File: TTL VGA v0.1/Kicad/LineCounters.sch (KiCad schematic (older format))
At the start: 17 parts

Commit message: tweaks
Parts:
- removed U? (x2): G22V10, symbol Logic_Programmable:PAL20RS10
- added U1, U5: G22V10, symbol 22V10:G22V10
- gave numbers to parts that had none: 9
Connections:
- net labels added: Aenable, ~AddressEnable
- wire segments 136 -> 145
- no-connect marks 4 -> 18
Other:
- moved on the sheet: U2B, U3B, U4B

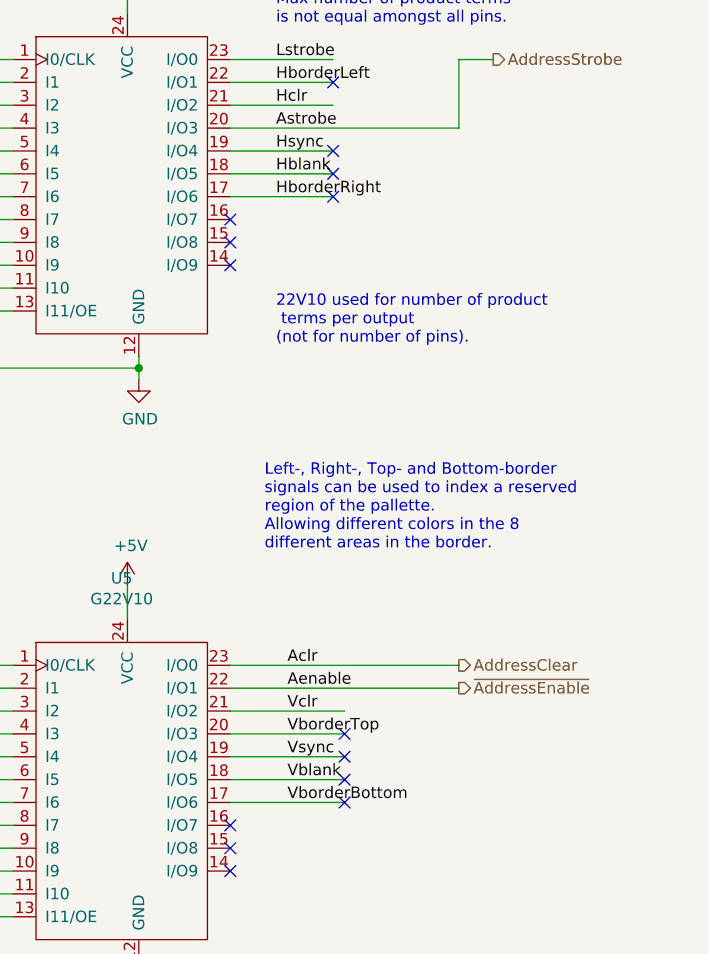
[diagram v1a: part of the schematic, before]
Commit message: vga memory interface
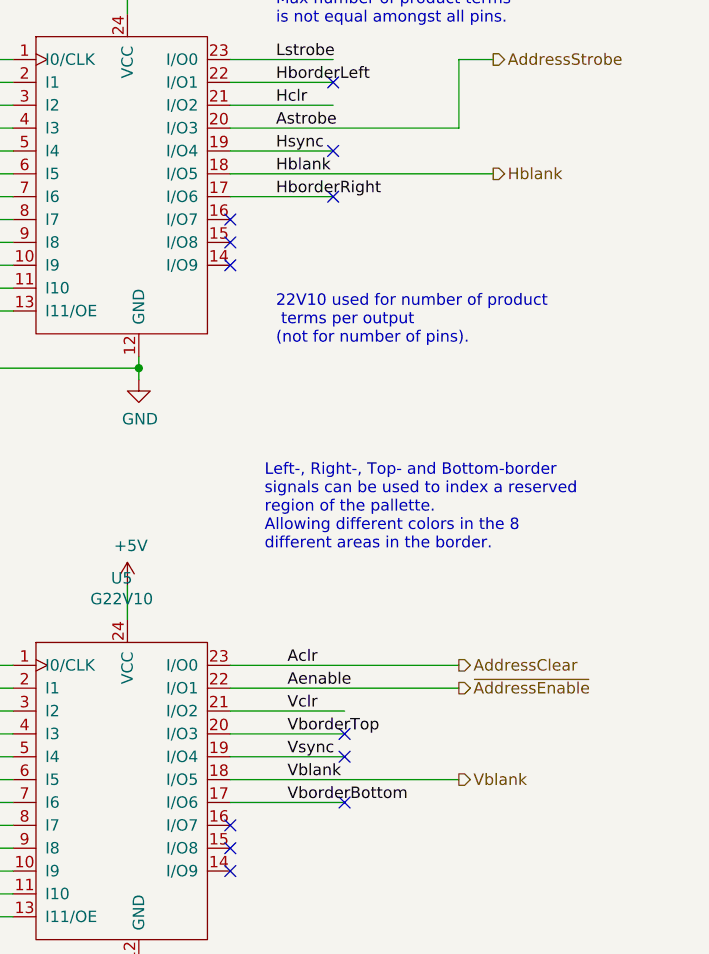
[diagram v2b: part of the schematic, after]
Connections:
- no-connect marks 18 -> 16
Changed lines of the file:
@@
 	1700 2150 1700 2300
-Wire Wire Line
-	9100 1950 9550 1950
 Wire Wire Line
 	9100 1550 9550 1550
@@
 Wire Wire Line
 	9100 4500 9600 4500
-Wire Wire Line
-	9100 4600 9600 4600
 Wire Wire Line
 	9100 4700 9600 4700
@@
 NoConn ~ 9100 2150
 NoConn ~ 9550 2050
-NoConn ~ 9550 1950
 NoConn ~ 9550 1850
 NoConn ~ 9550 1550
@@
 NoConn ~ 9100 4800
 NoConn ~ 9600 4700
-NoConn ~ 9600 4600
 NoConn ~ 9600 4500
 NoConn ~ 9600 4400
@@
 Wire Wire Line
 	4650 7050 4650 7250
+Text HLabel 10250 1950 2    50   Output ~ 0
+Hblank
+Text HLabel 10100 4600 2    50   Output ~ 0
+Vblank
+Wire Wire Line
+	9100 4600 10100 4600
+Wire Wire Line
+	9100 1950 10250 1950
 Wire Bus Line
 	7000 4000 7000 4550
